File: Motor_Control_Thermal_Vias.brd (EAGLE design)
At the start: 99.1 x 49.8 mm, 33 parts, among them J1 63971-1-QC_TAB-RA, J2 63971-1-QC_TAB-RA, J3 63971-1-QC_TAB-RA, J4 63971-1-QC_TAB-RA, Q1 FBDL0120N40-MO-299A, Q2 FBDL0120N40-MO-299A, Q3 FBDL0120N40-MO-299A, Q4 FBDL0120N40-MO-299A, U1 A3941-TSSOP28-LP

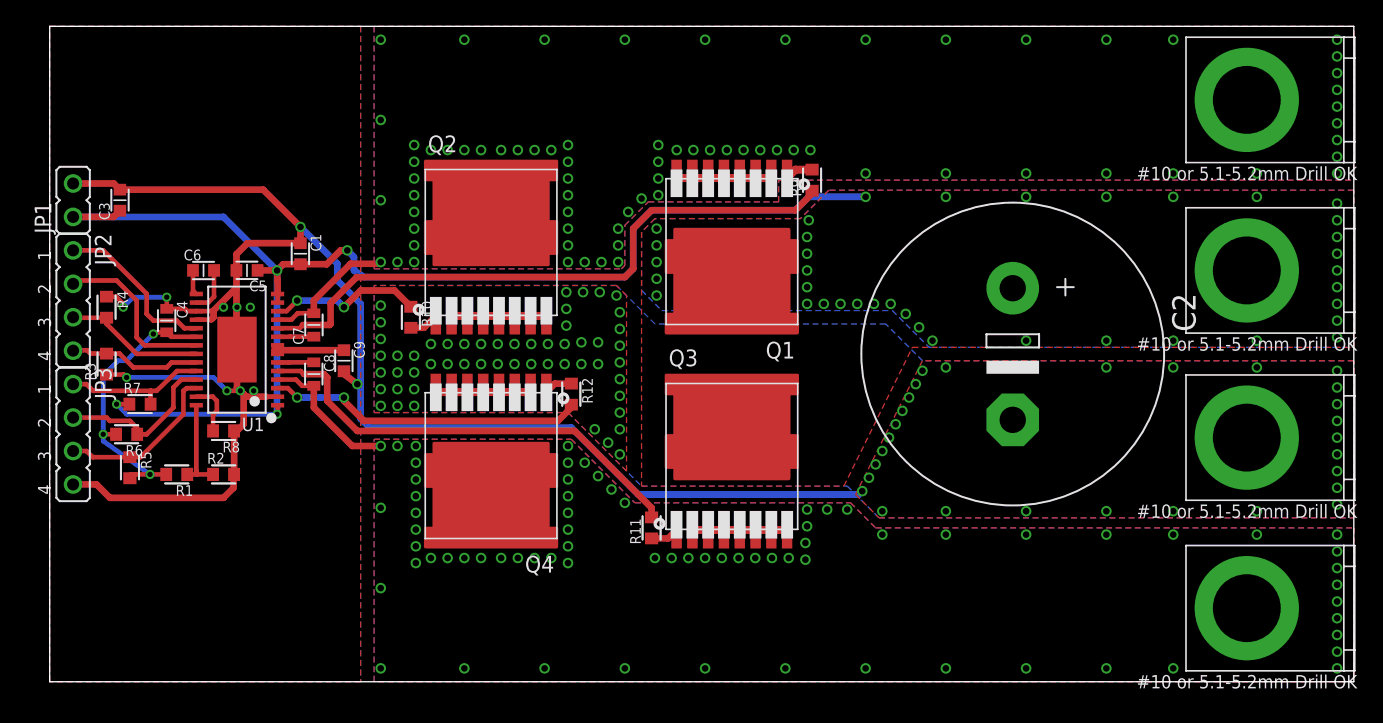
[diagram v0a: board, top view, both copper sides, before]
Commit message: More Via's!
It can't be a bad thing to add more via's to improve thermals. I also
added another CAP to improve noise. Silkscreen is updated and the board
is ready for production!
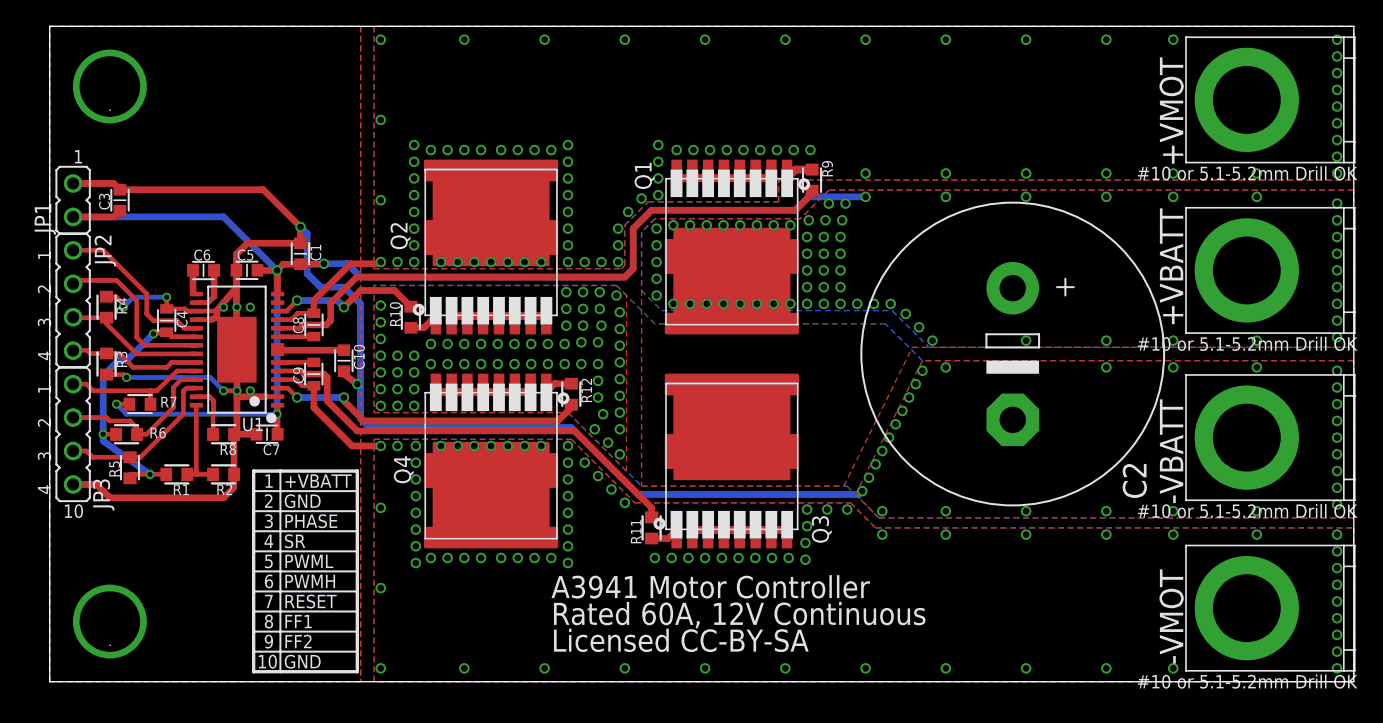
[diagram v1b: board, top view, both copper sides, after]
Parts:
- added C10: 4.7uF, Motor_Control:CAPC1608X92N
- added SCREW1, SCREW2: SCREW-4MM, Motor_Control:PLATEDSCREW-4MM
- C7: value 0.22uF -> 0.1uF; device Motor_Control:CAPC_0603_LONG -> Motor_Control:CAPC1608X92N
- C9: value 4.7uF -> 0.22uF; device Motor_Control:CAPC1608X92N -> Motor_Control:CAPC_0603_LONG
- moved C7 9.04 mm to (16.5, 18.8), turned to 180 degrees
- moved C8 3.73 mm to (20.1, 27.1), turned to 90 degrees
- moved C9 2.50 mm to (20.1, 23.4)
- moved R8 0.25 mm to (13.2, 18.8)
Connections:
- net +VBATT: now also C7.1
- net GND: now also C10.2, C7.2; no longer C9.2
- net N$15: now also C9.1; no longer C8.1
- net N$5: now also C10.1; no longer C9.1
- net N$6: now also C8.1; no longer C7.1
- net SA: now also C8.2; no longer C7.2
- net SB: now also C9.2; no longer C8.2
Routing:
- net GND: track 157.6 -> 160.3 mm, vias 95 -> 102
- net +VBATT: track 101.0 -> 101.2 mm, vias 42 -> 70
- net SB: vias 73 -> 80
- net SA: vias 74 -> 81
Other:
- board text added: "+VBATT"
- board text added: "+VMOT"
- board text added: "-VBATT"
- board text added: "-VMOT"
- board text added: "1"
- board text added: "10"
- board text added: "2"
- board text added: "3"
- board text added: "4"
- board text added: "5"
- board text added: "6"
- board text added: "7"
- board text added: "8"
- board text added: "9"
- board text added: "A3941 Motor Controller"
- board text added: "FF1"
- board text added: "FF2"
- board text added: "GND"
- board text added: "Licensed CC-BY-SA"
- board text added: "PHASE"
- board text added: "PWMH"
- board text added: "PWML"
- board text added: "RESET"
- board text added: "Rated 60A, 12V Continuous"
- board text added: "SR"
